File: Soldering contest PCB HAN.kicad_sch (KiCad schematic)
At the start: 13 parts, among them J1 Screw_Terminal_01x02, Q1 BC817, Q2 2N3904

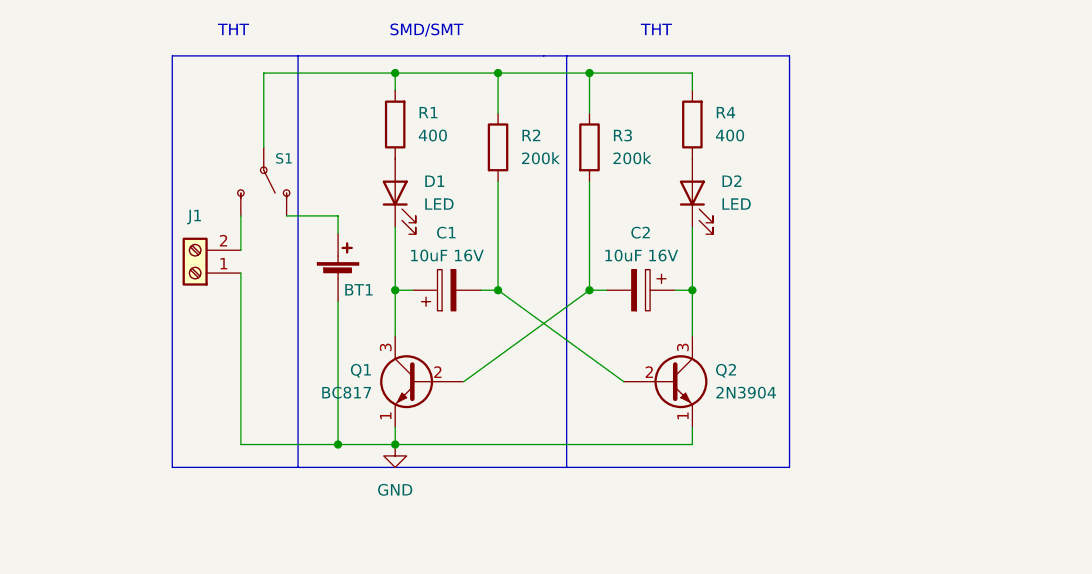
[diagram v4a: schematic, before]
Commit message: Added the correct values to the components
-R val
-C val
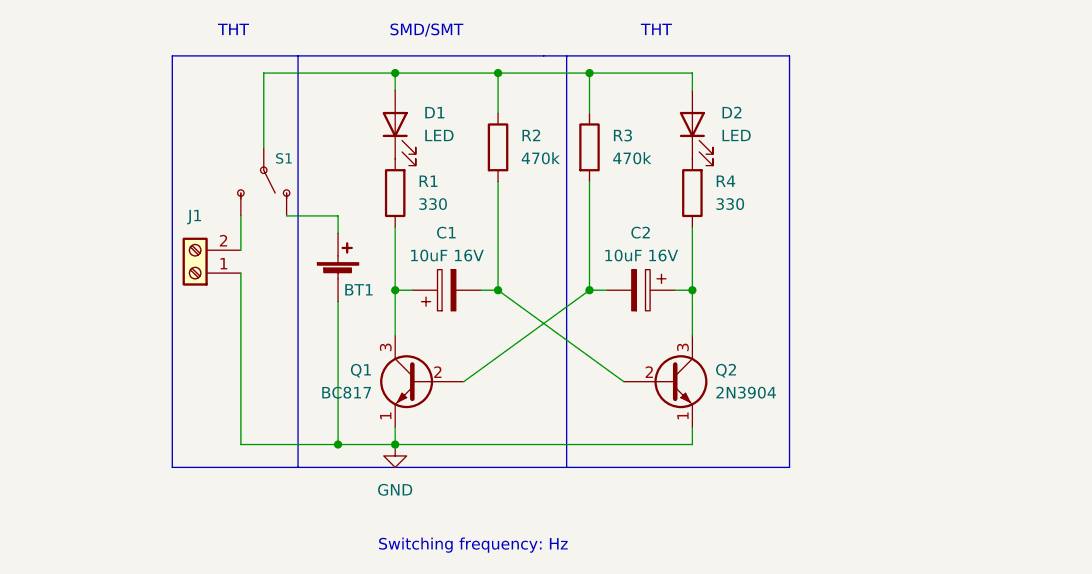
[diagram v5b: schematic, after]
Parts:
- R1, R4: value 400 -> 330
- R2, R3: value 200k -> 470k
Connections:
- net at C2.1, Q2.3 (C): now also R4.1; no longer D2.1 (K)
- net at D2.2 (A): now also D1.2 (A), R2.1, R3.1, S1.2 (P); no longer R4.1
- net at C1.1, Q1.3 (C): now also R1.1; no longer D1.1 (K)
- new net: D2.1 (K), R4.2
- new net: D1.1 (K), R1.2
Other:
- note added: "Switching frequency: Hz"
- moved on the sheet: D1, D2, R1, R4
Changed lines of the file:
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@@
   (title_block
     (title "Soldering contest PCB HAN")
-    (date "2022-11-18")
+    (date "2022-11-21")
     (rev "V0.2")
     (company "HAN ")
@@
     (effects (font (size 1.27 1.27)) (justify left bottom))
   )
-  (symbol (lib_id "Device:LED") (at 128.27 59.69 90) (unit 1)
-    (in_bom yes) (on_board yes)
-    (property "Reference" "D2" (id 0) (at 131.445 58.42 90)
-      (effects (font (size 1.27 1.27)) (justify right))
-    )
-    (property "Value" "LED" (id 1) (at 131.445 60.96 90)
-      (effects (font (size 1.27 1.27)) (justify right))
-    )
-    (property "Footprint" "LED_THT:LED_D5.0mm_Clear" (id 2) (at 128.27 59.69 0)
-      (effects (font (size 1.27 1.27)) hide)
-    )
-    (property "Datasheet" "~" (id 3) (at 128.27 59.69 0)
+  (text "Switching frequency: Hz" (at 93.345 99.695 0)
+    (effects (font (size 1.27 1.27)) (justify left bottom))
+  )
+  (symbol (lib_id "Device:LED") (at 128.27 52.07 90) (unit 1)
+    (in_bom yes) (on_board yes)
+    (property "Reference" "D2" (id 0) (at 131.445 50.8 90)
+      (effects (font (size 1.27 1.27)) (justify right))
+    )
+    (property "Value" "LED" (id 1) (at 131.445 53.34 90)
+      (effects (font (size 1.27 1.27)) (justify right))
+    )
+    (property "Footprint" "LED_THT:LED_D5.0mm_Clear" (id 2) (at 128.27 52.07 0)
+      (effects (font (size 1.27 1.27)) hide)
+    )
+    (property "Datasheet" "~" (id 3) (at 128.27 52.07 0)
       (effects (font (size 1.27 1.27)) hide)
     )
@@
     (pin "2")
   )
-  (symbol (lib_id "Device:R") (at 128.27 52.07 180) (unit 1)
-    (in_bom yes) (on_board yes) (fields_autoplaced)
-    (property "Reference" "R4" (id 0) (at 130.81 50.7999 0)
-      (effects (font (size 1.27 1.27)) (justify right))
-    )
-    (property "Value" "400" (id 1) (at 130.81 53.3399 0)
-      (effects (font (size 1.27 1.27)) (justify right))
-    )
-    (property "Footprint" "Resistor_THT:R_Axial_DIN0207_L6.3mm_D2.5mm_P7.62mm_Horizontal" (id 2) (at 130.048 52.07 90)
-      (effects (font (size 1.27 1.27)) hide)
-    )
-    (property "Datasheet" "~" (id 3) (at 128.27 52.07 0)
+  (symbol (lib_id "Device:R") (at 128.27 59.69 180) (unit 1)
+    (in_bom yes) (on_board yes) (fields_autoplaced)
+    (property "Reference" "R4" (id 0) (at 130.81 58.4199 0)
+      (effects (font (size 1.27 1.27)) (justify right))
+    )
+    (property "Value" "330" (id 1) (at 130.81 60.9599 0)
+      (effects (font (size 1.27 1.27)) (justify right))
+    )
+    (property "Footprint" "Resistor_THT:R_Axial_DIN0207_L6.3mm_D2.5mm_P7.62mm_Horizontal" (id 2) (at 130.048 59.69 90)
+      (effects (font (size 1.27 1.27)) hide)
+    )
+    (property "Datasheet" "~" (id 3) (at 128.27 59.69 0)
       (effects (font (size 1.27 1.27)) hide)
     )
@@
       (effects (font (size 1.27 1.27)) (justify left))
     )
-    (property "Value" "200k" (id 1) (at 109.22 55.8799 0)
+    (property "Value" "470k" (id 1) (at 109.22 55.8799 0)
       (effects (font (size 1.27 1.27)) (justify left))
     )
@@
       (effects (font (size 1.27 1.27)) (justify left))
     )
-    (property "Value" "200k" (id 1) (at 119.38 55.8799 0)
+    (property "Value" "470k" (id 1) (at 119.38 55.8799 0)
       (effects (font (size 1.27 1.27)) (justify left))
     )
@@
     (pin "3")
   )
-  (symbol (lib_id "Device:LED") (at 95.25 59.69 90) (unit 1)
-    (in_bom yes) (on_board yes)
-    (property "Reference" "D1" (id 0) (at 98.425 58.42 90)
-      (effects (font (size 1.27 1.27)) (justify right))
-    )
-    (property "Value" "LED" (id 1) (at 98.425 60.96 90)
-      (effects (font (size 1.27 1.27)) (justify right))
-    )
-    (property "Footprint" "LED_SMD:LED_0805_2012Metric_Pad1.15x1.40mm_HandSolder" (id 2) (at 95.25 59.69 0)
+  (symbol (lib_id "Device:LED") (at 95.25 52.07 90) (unit 1)
+    (in_bom yes) (on_board yes)
+    (property "Reference" "D1" (id 0) (at 98.425 50.8 90)
+      (effects (font (size 1.27 1.27)) (justify right))
+    )
+    (property "Value" "LED" (id 1) (at 98.425 53.34 90)
+      (effects (font (size 1.27 1.27)) (justify right))
+    )
+    (property "Footprint" "LED_SMD:LED_0805_2012Metric_Pad1.15x1.40mm_HandSolder" (id 2) (at 95.25 52.07 0)
+      (effects (font (size 1.27 1.27)) hide)
+    )
+    (property "Datasheet" "~" (id 3) (at 95.25 52.07 0)
+      (effects (font (size 1.27 1.27)) hide)
+    )
+    (pin "1")
+    (pin "2")
+  )
+  (symbol (lib_id "Device:R") (at 95.25 59.69 180) (unit 1)
+    (in_bom yes) (on_board yes) (fields_autoplaced)
+    (property "Reference" "R1" (id 0) (at 97.79 58.4199 0)
+      (effects (font (size 1.27 1.27)) (justify right))
+    )
+    (property "Value" "330" (id 1) (at 97.79 60.9599 0)
+      (effects (font (size 1.27 1.27)) (justify right))
+    )
+    (property "Footprint" "Resistor_SMD:R_01005_0402Metric_Pad0.57x0.30mm_HandSolder" (id 2) (at 97.028 59.69 90)
       (effects (font (size 1.27 1.27)) hide)
     )
     (property "Datasheet" "~" (id 3) (at 95.25 59.69 0)
-      (effects (font (size 1.27 1.27)) hide)
-    )
-    (pin "1")
-    (pin "2")
-  )
-  (symbol (lib_id "Device:R") (at 95.25 52.07 180) (unit 1)
-    (in_bom yes) (on_board yes) (fields_autoplaced)
-    (property "Reference" "R1" (id 0) (at 97.79 50.7999 0)
-      (effects (font (size 1.27 1.27)) (justify right))
-    )
-    (property "Value" "400" (id 1) (at 97.79 53.3399 0)
-      (effects (font (size 1.27 1.27)) (justify right))
-    )
-    (property "Footprint" "Resistor_SMD:R_01005_0402Metric_Pad0.57x0.30mm_HandSolder" (id 2) (at 97.028 52.07 90)
-      (effects (font (size 1.27 1.27)) hide)
-    )
-    (property "Datasheet" "~" (id 3) (at 95.25 52.07 0)
       (effects (font (size 1.27 1.27)) hide)
     )
@@
     )
     (path "/d18fc897-0878-42f5-b8a2-449363703de6"
-      (reference "R1") (unit 1) (value "400") (footprint "Resistor_SMD:R_01005_0402Metric_Pad0.57x0.30mm_HandSolder")
+      (reference "R1") (unit 1) (value "330") (footprint "Resistor_SMD:R_01005_0402Metric_Pad0.57x0.30mm_HandSolder")
     )
     (path "/5eba335f-f9b7-4f96-8244-9f11f5b02fc1"
-      (reference "R2") (unit 1) (value "200k") (footprint "Resistor_SMD:R_0805_2012Metric_Pad1.20x1.40mm_HandSolder")
+      (reference "R2") (unit 1) (value "470k") (footprint "Resistor_SMD:R_0805_2012Metric_Pad1.20x1.40mm_HandSolder")
     )
     (path "/5fd75fa8-c971-4180-8d4d-419bf5fd463a"
-      (reference "R3") (unit 1) (value "200k") (footprint "Resistor_THT:R_Axial_DIN0204_L3.6mm_D1.6mm_P2.54mm_Vertical")
+      (reference "R3") (unit 1) (value "470k") (footprint "Resistor_THT:R_Axial_DIN0204_L3.6mm_D1.6mm_P2.54mm_Vertical")
     )
     (path "/22a04216-54cb-44fe-9b76-e181b36e1a9f"
-      (reference "R4") (unit 1) (value "400") (footprint "Resistor_THT:R_Axial_DIN0207_L6.3mm_D2.5mm_P7.62mm_Horizontal")
+      (reference "R4") (unit 1) (value "330") (footprint "Resistor_THT:R_Axial_DIN0207_L6.3mm_D2.5mm_P7.62mm_Horizontal")
     )
     (path "/6502d947-661b-4d45-91f3-16aac5eae88a"

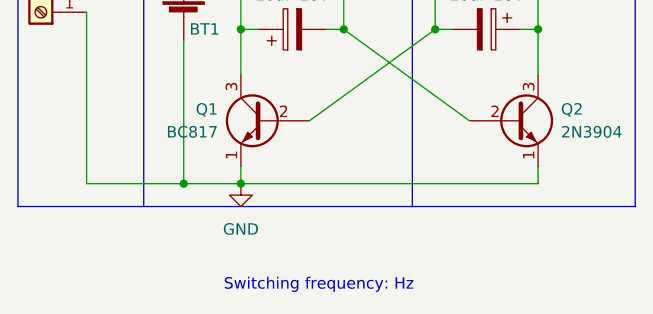
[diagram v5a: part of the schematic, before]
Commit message: Finished V0.2
-added interactive BOM
-added improved schematic
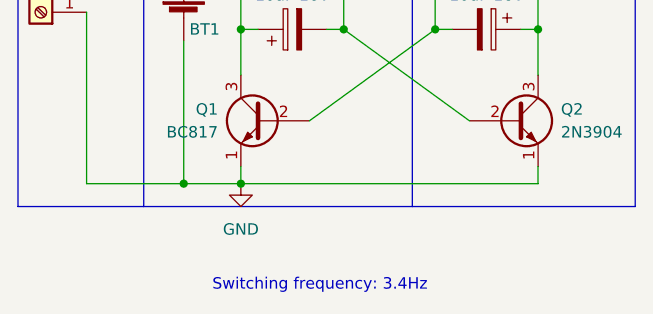
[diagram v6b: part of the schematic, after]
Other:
- note added: "Switching frequency: 3.4Hz"
- note removed: "Switching frequency: Hz"
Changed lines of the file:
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@@
     (effects (font (size 1.27 1.27)) (justify left bottom))
   )
-  (text "Switching frequency: Hz" (at 93.345 99.695 0)
+  (text "Switching frequency: 3.4Hz" (at 92.075 99.695 0)
     (effects (font (size 1.27 1.27)) (justify left bottom))
   )

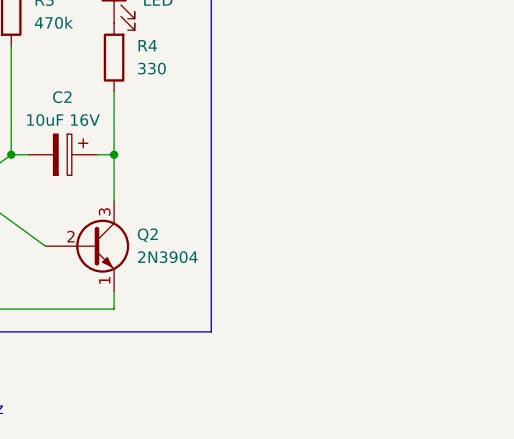
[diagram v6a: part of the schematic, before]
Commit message: enh board
-added mounting holes
-updated silkscreen date
-changed R1 footprint to match ERC
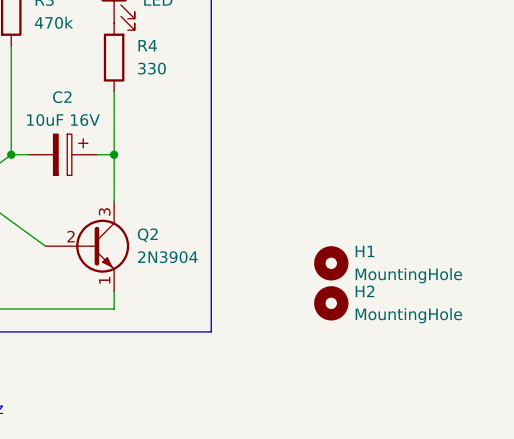
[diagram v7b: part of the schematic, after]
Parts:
- added H1, H2: MountingHole, MountingHole:MountingHole_4.3mm_M4, symbol Mechanical:MountingHole
- R1: footprint Resistor_SMD:R_01005_0402Metric_Pad0.57x0.30mm_HandSolder -> Resistor_SMD:R_0402_1005Metric
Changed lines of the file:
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@@
     (pin "2")
+  )
+  (symbol (lib_id "Mechanical:MountingHole") (at 152.4 86.995 0) (unit 1)
+    (in_bom yes) (on_board yes) (fields_autoplaced)
+    (property "Reference" "H2" (id 0) (at 154.94 85.7249 0)
+      (effects (font (size 1.27 1.27)) (justify left))
+    )
+    (property "Value" "MountingHole" (id 1) (at 154.94 88.2649 0)
+      (effects (font (size 1.27 1.27)) (justify left))
+    )
+    (property "Footprint" "MountingHole:MountingHole_4.3mm_M4" (id 2) (at 152.4 86.995 0)
+      (effects (font (size 1.27 1.27)) hide)
+    )
+    (property "Datasheet" "~" (id 3) (at 152.4 86.995 0)
+      (effects (font (size 1.27 1.27)) hide)
+    )
   )
   (symbol (lib_id "Device:C_Polarized") (at 100.965 70.485 90) (unit 1)
@@
     (pin "3")
   )
+  (symbol (lib_id "Mechanical:MountingHole") (at 152.4 82.55 0) (unit 1)
+    (in_bom yes) (on_board yes) (fields_autoplaced)
+    (property "Reference" "H1" (id 0) (at 154.94 81.2799 0)
+      (effects (font (size 1.27 1.27)) (justify left))
+    )
+    (property "Value" "MountingHole" (id 1) (at 154.94 83.8199 0)
+      (effects (font (size 1.27 1.27)) (justify left))
+    )
+    (property "Footprint" "MountingHole:MountingHole_4.3mm_M4" (id 2) (at 152.4 82.55 0)
+      (effects (font (size 1.27 1.27)) hide)
+    )
+    (property "Datasheet" "~" (id 3) (at 152.4 82.55 0)
+      (effects (font (size 1.27 1.27)) hide)
+    )
+  )
   (symbol (lib_id "Device:LED") (at 95.25 52.07 90) (unit 1)
     (in_bom yes) (on_board yes)
@@
       (effects (font (size 1.27 1.27)) (justify right))
     )
-    (property "Footprint" "Resistor_SMD:R_01005_0402Metric_Pad0.57x0.30mm_HandSolder" (id 2) (at 97.028 59.69 90)
+    (property "Footprint" "Resistor_SMD:R_0402_1005Metric" (id 2) (at 97.028 59.69 90)
       (effects (font (size 1.27 1.27)) hide)
     )
@@
       (reference "D2") (unit 1) (value "LED") (footprint "LED_THT:LED_D5.0mm_Clear")
     )
+    (path "/a56f4f37-3859-41b2-a969-dc810cea9776"
+      (reference "H1") (unit 1) (value "MountingHole") (footprint "MountingHole:MountingHole_4.3mm_M4")
+    )
+    (path "/33cbc48d-7a21-48d6-b9b7-57e0684786a6"
+      (reference "H2") (unit 1) (value "MountingHole") (footprint "MountingHole:MountingHole_4.3mm_M4")
+    )
     (path "/0fe9d6fd-bdce-4016-adb7-83a4c7c35634"
       (reference "J1") (unit 1) (value "Screw_Terminal_01x02") (footprint "TerminalBlock:TerminalBlock_bornier-2_P5.08mm")
@@
     )
     (path "/d18fc897-0878-42f5-b8a2-449363703de6"
-      (reference "R1") (unit 1) (value "330") (footprint "Resistor_SMD:R_01005_0402Metric_Pad0.57x0.30mm_HandSolder")
+      (reference "R1") (unit 1) (value "330") (footprint "Resistor_SMD:R_0402_1005Metric")
     )
     (path "/5eba335f-f9b7-4f96-8244-9f11f5b02fc1"

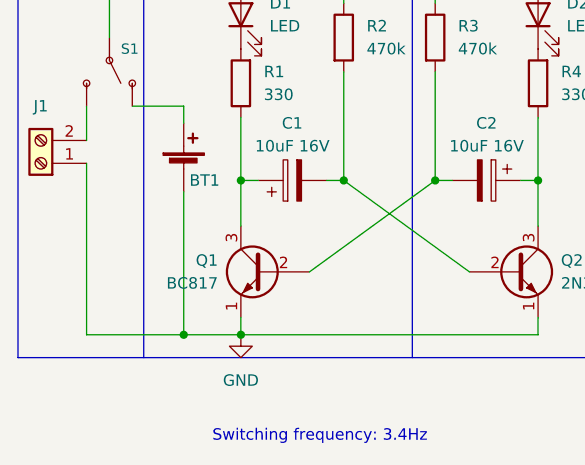
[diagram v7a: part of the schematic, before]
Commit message: Updated component
BC817 -> BC817R
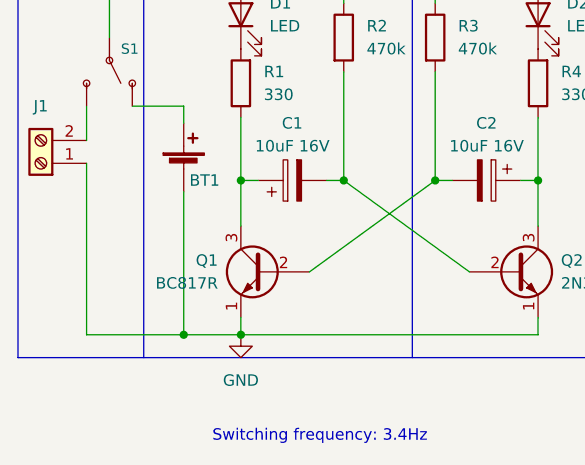
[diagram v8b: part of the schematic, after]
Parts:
- Q1: value BC817 -> BC817R
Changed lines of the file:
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@@
   (title_block
     (title "Soldering contest PCB HAN")
-    (date "2022-11-21")
-    (rev "V0.2")
+    (date "2023-01-26")
+    (rev "V0.3")
     (company "HAN ")
     (comment 1 "Designed by: Casper R. Tak")
@@
       (effects (font (size 1.27 1.27)) (justify left))
     )
-    (property "Value" "BC817" (id 1) (at 92.71 81.9149 0)
+    (property "Value" "BC817R" (id 1) (at 92.71 81.9149 0)
       (effects (font (size 1.27 1.27)) (justify left))
     )
@@
     )
     (path "/6b424259-f8a0-4482-996c-adc9565aa863"
-      (reference "Q1") (unit 1) (value "BC817") (footprint "Package_TO_SOT_SMD:SOT-23_Handsoldering")
+      (reference "Q1") (unit 1) (value "BC817R") (footprint "Package_TO_SOT_SMD:SOT-23_Handsoldering")
     )
     (path "/0fd58cd3-0637-4e39-b339-0859c358a065"
